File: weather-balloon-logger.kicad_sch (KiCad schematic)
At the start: 12 parts, among them J1 LightHAB VBATT/GND, J2 LightHABTracker 1.0, J3 LightHAB OUT1/GND, J5 Cutdown output

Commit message: feat(lighthab): finish carrier migration
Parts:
- A1: MPN (none) -> DEV-13955
- A2: MPN (none) -> Pololu item 2123
- C1: MPN (none) -> C322C475K5R5TA
- C2: MPN (none) -> C315C104K5R5TA
- D1: MPN (none) -> WP710A10SGC
- J1: MPN (none) -> TBD-LightHAB-VBATT
- J2: MPN (none) -> TBD-LightHAB-1x9
- J3: MPN (none) -> TBD-LightHAB-OUT1
- J5: MPN (none) -> S2B-XH-A(LF)(SN)
- R1, R4: MPN (none) -> MFR-25FBF52-1K
- R2: MPN (none) -> MFR-25FBF52-100K
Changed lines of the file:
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@@
+			(effects (font (size 1.27 1.27)) hide)
+		)
+		(property "MPN" "DEV-13955" (at 214.63 128.27 0)
 			(effects (font (size 1.27 1.27)) hide)
 		)
@@
 			(effects (font (size 1.27 1.27)) hide)
 		)
+		(property "MPN" "Pololu item 2123" (at 95.25 127 0)
+			(effects (font (size 1.27 1.27)) hide)
+		)
 		(pin "1")
 		(pin "2")
@@
 			(effects (font (size 1.27 1.27)) hide)
 		)
+		(property "MPN" "C322C475K5R5TA" (at 233.68 128.27 0)
+			(effects (font (size 1.27 1.27)) hide)
+		)
 		(pin "1")
 		(pin "2")
@@
 			(effects (font (size 1.27 1.27)) hide)
 		)
+		(property "MPN" "C315C104K5R5TA" (at 233.68 149.86 0)
+			(effects (font (size 1.27 1.27)) hide)
+		)
 		(pin "1")
 		(pin "2")
@@
 			(effects (font (size 1.27 1.27)) hide)
 		)
+		(property "MPN" "WP710A10SGC" (at 267.97 134.62 0)
+			(effects (font (size 1.27 1.27)) hide)
+		)
 		(pin "1")
 		(pin "2")
@@
 			(effects (font (size 1.27 1.27)) hide)
 		)
+		(property "MPN" "TBD-LightHAB-VBATT" (at 95.25 143.51 0)
+			(effects (font (size 1.27 1.27)) hide)
+		)
 		(pin "1")
 		(pin "2")
@@
 		)
 		(property "Datasheet" "~" (at 154.94 133.35 0)
+			(effects (font (size 1.27 1.27)) hide)
+		)
+		(property "MPN" "TBD-LightHAB-1x9" (at 154.94 133.35 0)
 			(effects (font (size 1.27 1.27)) hide)
 		)
@@
 			(effects (font (size 1.27 1.27)) hide)
 		)
+		(property "MPN" "TBD-LightHAB-OUT1" (at 321.31 123.19 0)
+			(effects (font (size 1.27 1.27)) hide)
+		)
 		(pin "1")
 		(pin "2")
@@
 			(effects (font (size 1.27 1.27)) hide)
 		)
+		(property "MPN" "S2B-XH-A(LF)(SN)" (at 321.31 137.16 0)
+			(effects (font (size 1.27 1.27)) hide)
+		)
 		(pin "1")
 		(pin "2")
@@
 			(effects (font (size 1.27 1.27)) hide)
 		)
+		(property "MPN" "MFR-25FBF52-1K" (at 274.32 125.73 0)
+			(effects (font (size 1.27 1.27)) hide)
+		)
 		(pin "1")
 		(pin "2")
@@
 			(effects (font (size 1.27 1.27)) hide)
 		)
+		(property "MPN" "MFR-25FBF52-100K" (at 287.02 160.02 0)
+			(effects (font (size 1.27 1.27)) hide)
+		)
 		(pin "1")
 		(pin "2")
@@
 			(effects (font (size 1.27 1.27)) hide)
 		)
+		(property "MPN" "MFR-25FBF52-1K" (at 189.23 133.35 0)
+			(effects (font (size 1.27 1.27)) hide)
+		)

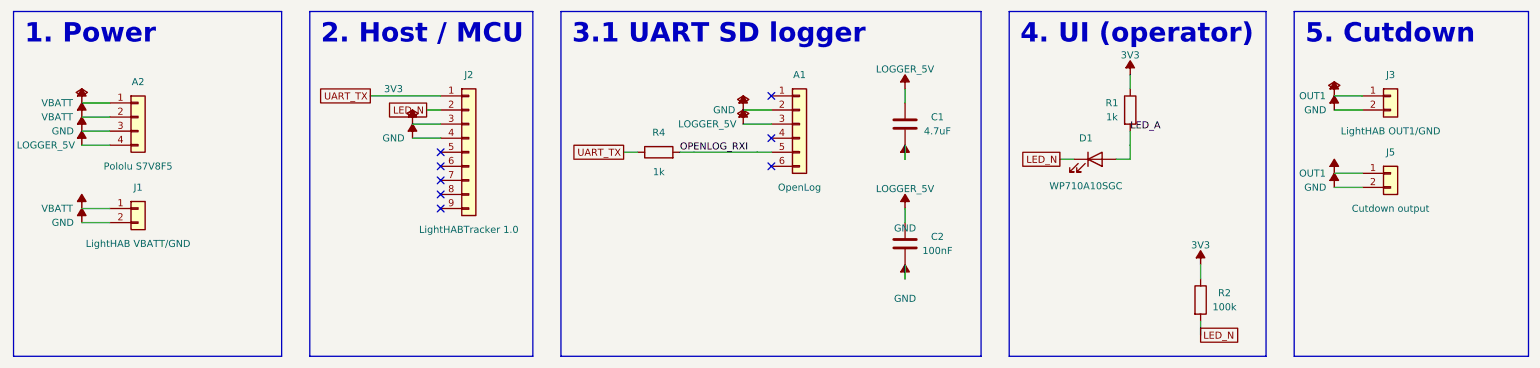
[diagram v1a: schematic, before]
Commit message: refactor(power): use LightHAB 3V3 for OpenLog
Remove the separate VBATT-fed regulator path. Keep host rail capacity as a bench-test gate before fabrication.
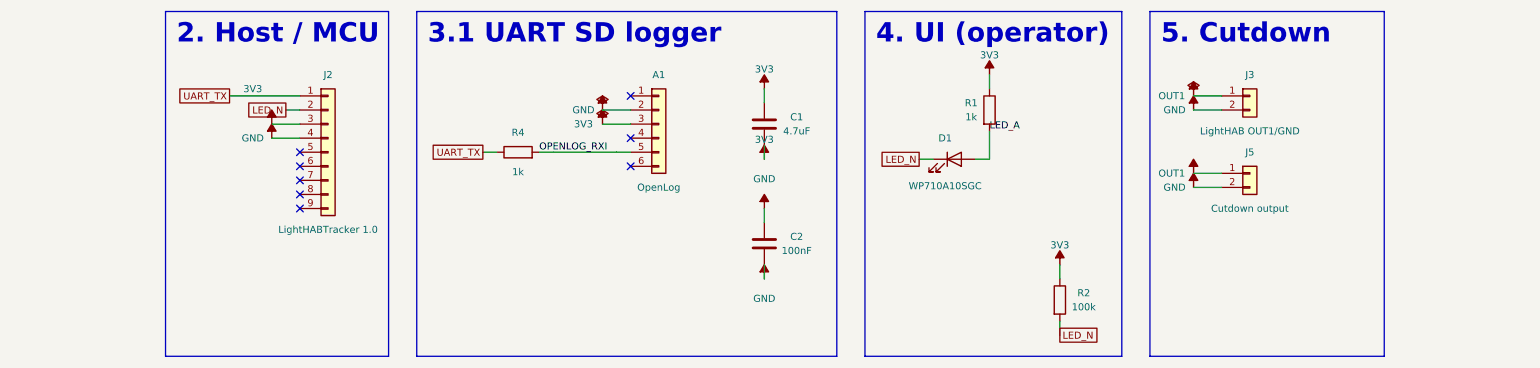
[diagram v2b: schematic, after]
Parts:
- removed A2: Pololu S7V8F5, WeatherBalloon:Pololu_S7V8F5_Carrier, symbol Connector_Generic:Conn_01x04
- removed J1: LightHAB VBATT/GND, Connector_PinHeader_2.54mm:PinHeader_1x02_P2.54mm_Vertical, symbol Connector_Generic:Conn_01x02
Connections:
- net LOGGER_5V is gone; now on net 3V3: A1.3 (Pin_3), C1.1, C2.1
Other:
- note removed: "1. Power"
- moved on the sheet: A1, C1, C2, D1, J2, J3, J5, R1, R2, R4
